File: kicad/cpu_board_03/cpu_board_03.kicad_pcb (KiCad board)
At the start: 2 copper layers, 99.1 x 94.2 mm, 65 parts, among them J1 DIN41612_02x32_AC, J11 Conn_01x09, J2 Clock, J6 Conn_01x02_Socket, J9 Ram1 Enable, SW1 SW_Reset, SW2 SW_PWR, U1 W65C02SxP, U10 74HC245, U13 74AHC1G32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

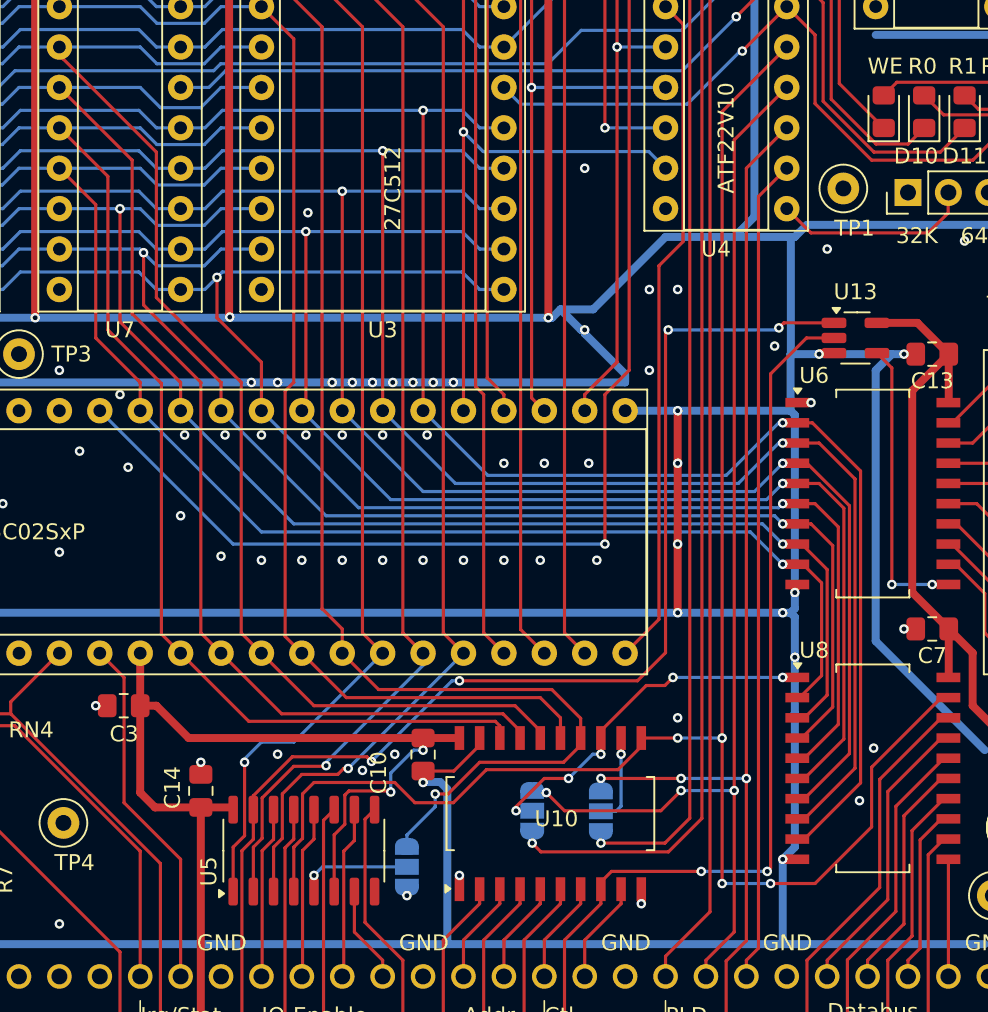
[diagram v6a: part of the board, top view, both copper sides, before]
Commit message: cpu board & backplane as ordered
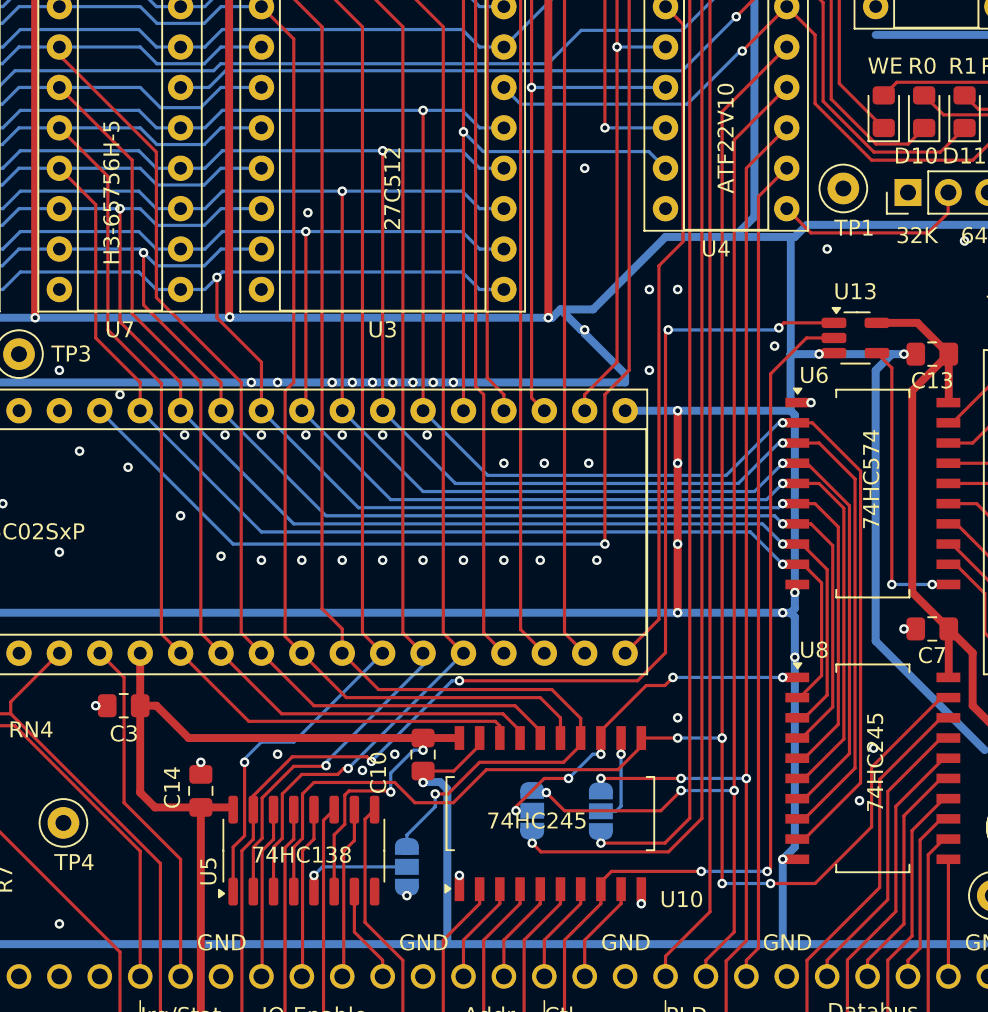
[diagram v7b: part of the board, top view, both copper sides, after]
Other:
- board text added: "74HC138"
- board text added: "74HC245"
- board text added: "74HC574"
- board text added: "A4"
- board text added: "H3-65756H-5"
- board text added: "O7"
- board text added: "O8"
- board text added: "~{OE}"
- board text added: "~{QWE}"
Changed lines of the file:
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@@
 		(tags "S0-20 ")
 		(property "Reference" "U10"
-			(at -0.33 0.381 0)
+			(at -5.41 8.255 0)
 			(layer "F.SilkS")
 			(effects
@@
 		)
 	)
+	(gr_text "74HC245\n"
+		(at 93.518001 86.756001 0)
+		(layer "F.SilkS")
+		(effects
+			(font
+				(size 1 1)
+				(thickness 0.15)
+			)
+		)
+	)
 	(gr_text "VCC"
 		(at 97.536 104.648 0)
@@
 		)
 	)
+	(gr_text "74HC245\n"
+		(at 114.808 83.058 90)
+		(layer "F.SilkS")
+		(effects
+			(font
+				(size 1 1)
+				(thickness 0.15)
+			)
+		)
+	)
 	(gr_text "Power"
 		(at 36.322 92.202 0)
@@
 		)
 	)
+	(gr_text "74HC574"
+		(at 114.554 65.278 90)
+		(layer "F.SilkS")
+		(effects
+			(font
+				(size 1 1)
+				(thickness 0.15)
+			)
+		)
+	)
+	(gr_text "H3-65756H-5"
+		(at 66.802 47.244 90)
+		(layer "F.SilkS")
+		(effects
+			(font
+				(size 1 1)
+				(thickness 0.15)
+			)
+		)
+	)
 	(gr_text "GND"
 		(at 120.396 94.996 0)
@@
 		)
 	)
+	(gr_text "74HC138\n"
+		(at 78.74 88.9 0)
+		(layer "F.SilkS")
+		(effects
+			(font
+				(size 1 1)
+				(thickness 0.15)
+			)
+		)
+	)
 	(gr_text "GND"
 		(at 97.536 94.996 0)
@@
 		)
 	)
+	(gr_text "A4"
+		(at 86.36 87.122 0)
+		(layer "B.SilkS")
+		(effects
+			(font
+				(size 1 1)
+				(thickness 0.1)
+			)
+			(justify left bottom mirror)
+		)
+	)
+	(gr_text "~{OE}"
+		(at 94.234 90.17 0)
+		(layer "B.SilkS")
+		(effects
+			(font
+				(size 1 1)
+				(thickness 0.1)
+			)
+			(justify left bottom mirror)
+		)
+	)
+	(gr_text "~{QWE}"
+		(at 99.06 90.17 0)
+		(layer "B.SilkS")
+		(effects
+			(font
+				(size 1 1)
+				(thickness 0.1)
+			)
+			(justify left bottom mirror)
+		)
+	)
+	(gr_text "PLD"
+		(at 96.52 82.296 0)
+		(layer "B.SilkS")
+		(effects
+			(font
+				(size 1 1)
+				(thickness 0.1)
+			)
+			(justify left bottom mirror)
+		)
+	)
+	(gr_text "O7"
+		(at 94.234 83.566 0)
+		(layer "B.SilkS")
+		(effects
+			(font
+				(size 1 1)
+				(thickness 0.1)
+			)
+			(justify left bottom mirror)
+		)
+	)
+	(gr_text "O8"
+		(at 98.552 83.566 0)
+		(layer "B.SilkS")
+		(effects
+			(font
+				(size 1 1)
+				(thickness 0.1)
+			)
+			(justify left bottom mirror)
+		)
+	)

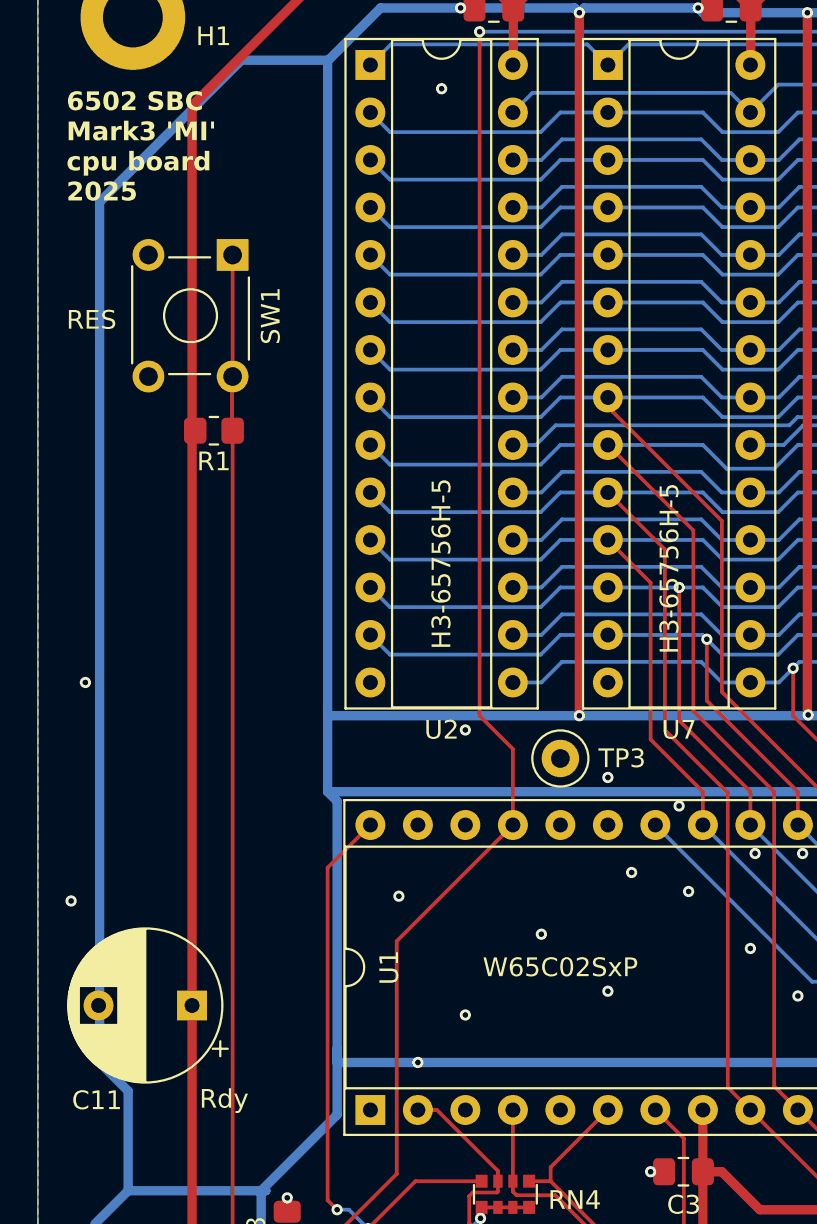
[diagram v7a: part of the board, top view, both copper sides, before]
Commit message: fix mark3 cpu board error: BE not connected
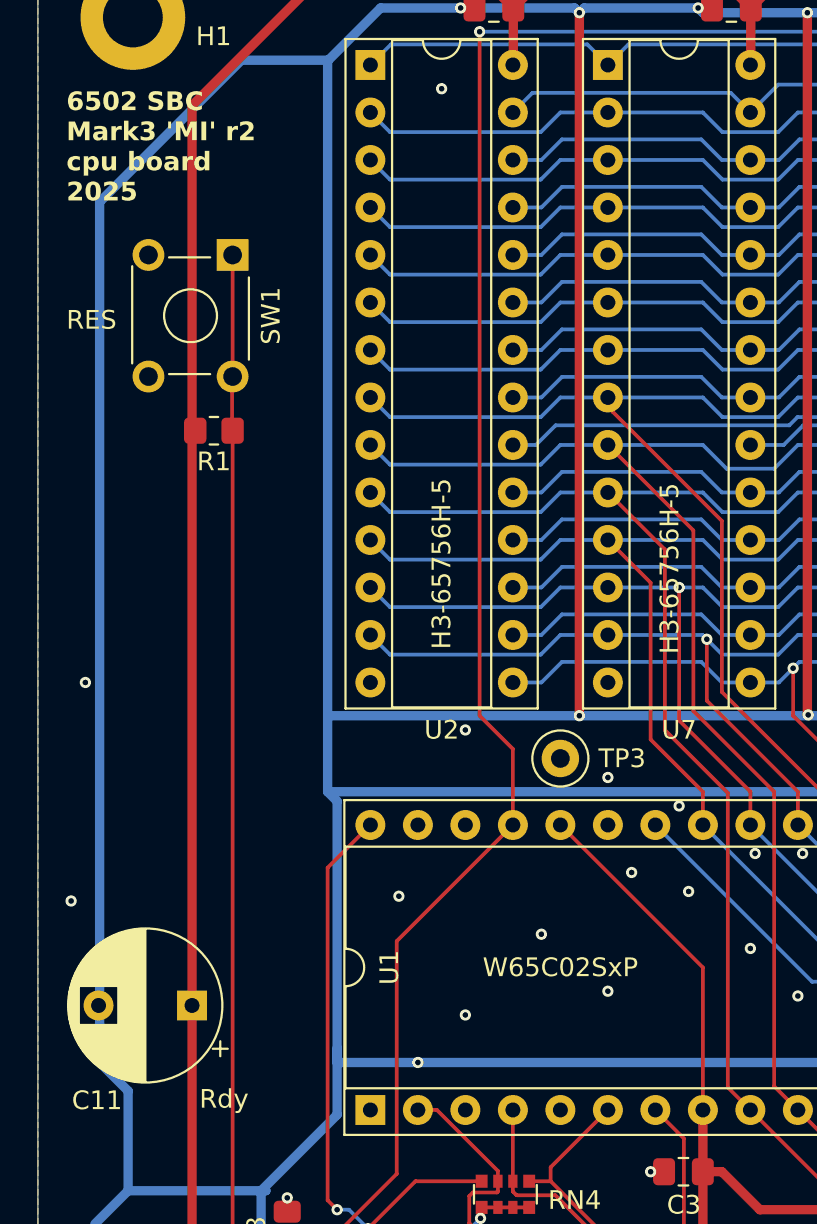
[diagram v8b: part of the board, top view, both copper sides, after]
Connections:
- U1 pad 36: unconnected-(U1-BE-Pad36) -> VCC
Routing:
- net VCC: track 480.3 -> 498.7 mm
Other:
- board text added: "6502 SBC Mark3 'MI' r2 cpu board 2025"
- board text removed: "6502 SBC Mark3 'MI' cpu board 2025"
